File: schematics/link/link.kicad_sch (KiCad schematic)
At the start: 22 parts, among them J1 S2, J2 ARJM11C7-114-BA-EW2, J3 SDI12, J4 S1

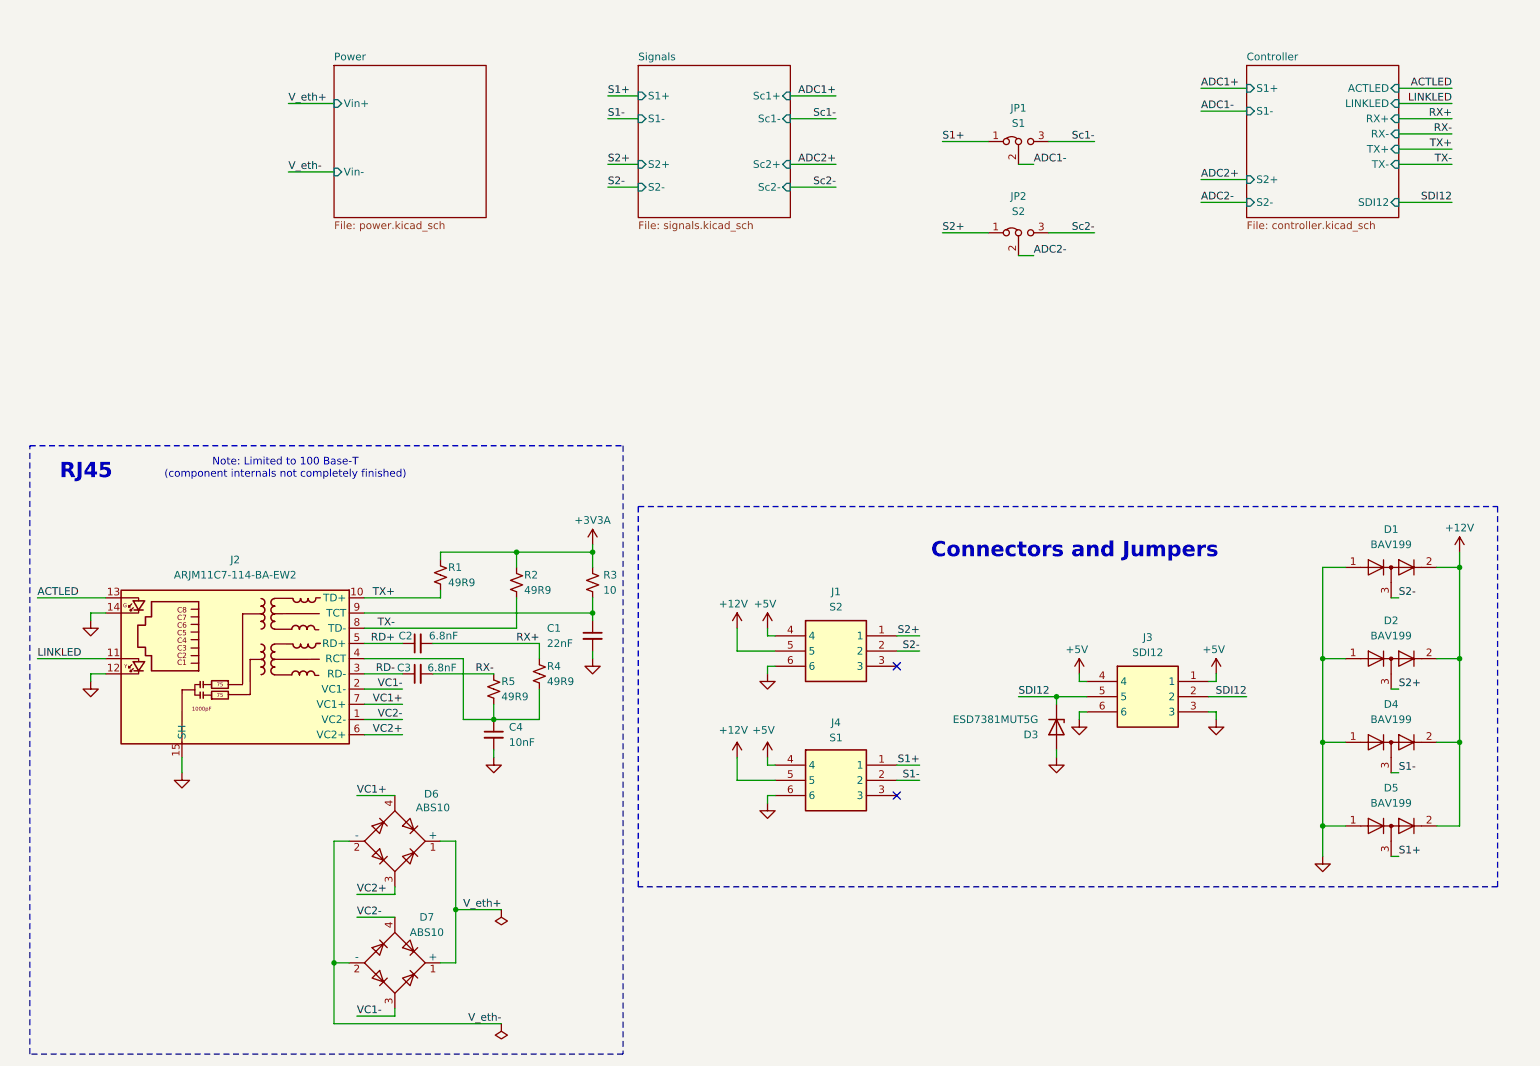
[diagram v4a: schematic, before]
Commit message: update(review):
1. Take gain resistor out of AFE filter
2. Breakout I2C
3. Move fuse to cover both 12V rails
4. Silkscreens
5. More testpoints + change to clip ons
6. Match ADC input max and filter output max
7. Add shunt for current resistors
8. Thermocouples
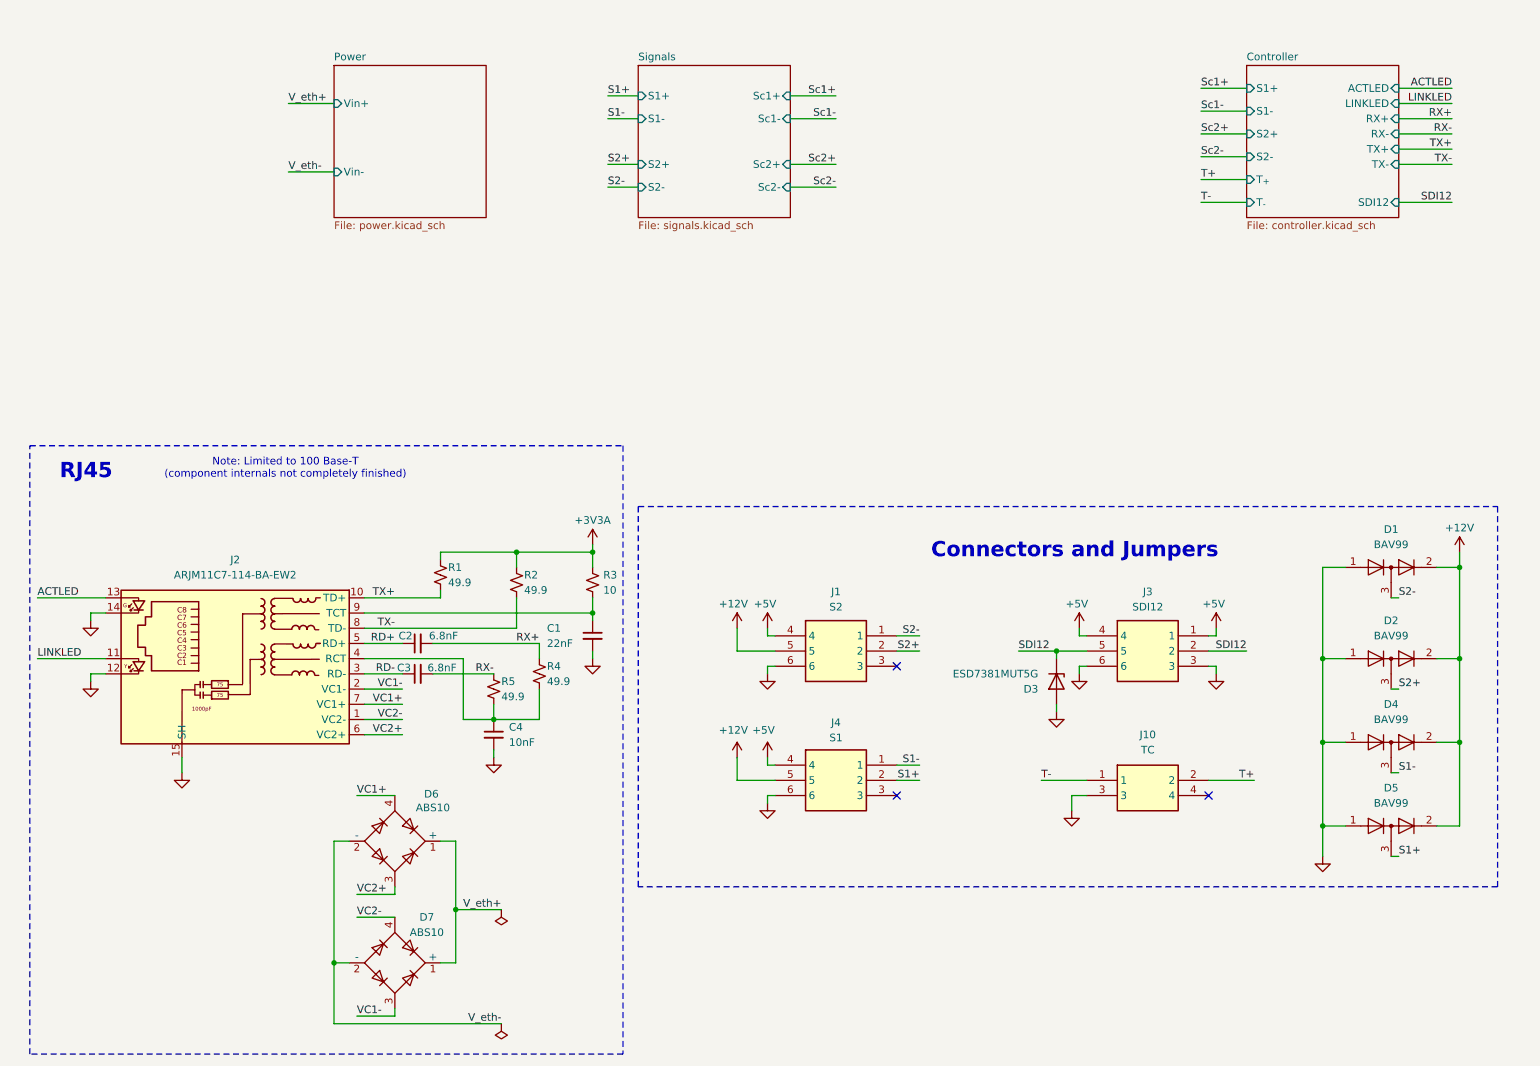
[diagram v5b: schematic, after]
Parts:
- removed JP1: S1, Connector_PinHeader_2.54mm:PinHeader_1x03_P2.54mm_Vertical, symbol Jumper:Jumper_3_Bridged12
- removed JP2: S2, Connector_PinHeader_2.54mm:PinHeader_1x03_P2.54mm_Vertical, symbol Jumper:Jumper_3_Bridged12
- added J10: TC, Link_Footprints:PC-1053864, symbol Link_Components:PC-1053864
- C1: MPN (none) -> GRM155R71H223JA12D
- C2, C3: MPN (none) -> GRM155R71E682KA01D
- C4: MPN (none) -> GRM155R71H103KA88D
- D1, D2, D4, D5: value BAV199 -> BAV99; MPN (none) -> BAV99
- D3: MPN (none) -> ESD7381MUT5G
- D6, D7: MPN (none) -> ABS10
- J1, J3, J4: MPN (none) -> 1053866
- J2: MPN (none) -> ARJM11C7-114-BA-EW2
- R1, R2, R4, R5: value 49R9 -> 49.9; MPN (none) -> RC0402FR-0749R9L
- R3: MPN (none) -> RC0402FR-0710RL
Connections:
- net GND: now also J10.3
- net S1+: now also J4.2; no longer J4.1
- net S1-: now also J4.1; no longer J4.2
- net S2+: now also J1.2; no longer J1.1
- net S2-: now also J1.1; no longer J1.2
- new net T+: J10.2
- new net T-: J10.1
- no-connect marks 2 -> 3
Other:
- sheet Controller ports: added T_{+}, T_{-}; removed none
- moved on the sheet: D3, J3

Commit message: update(connector pinouts)
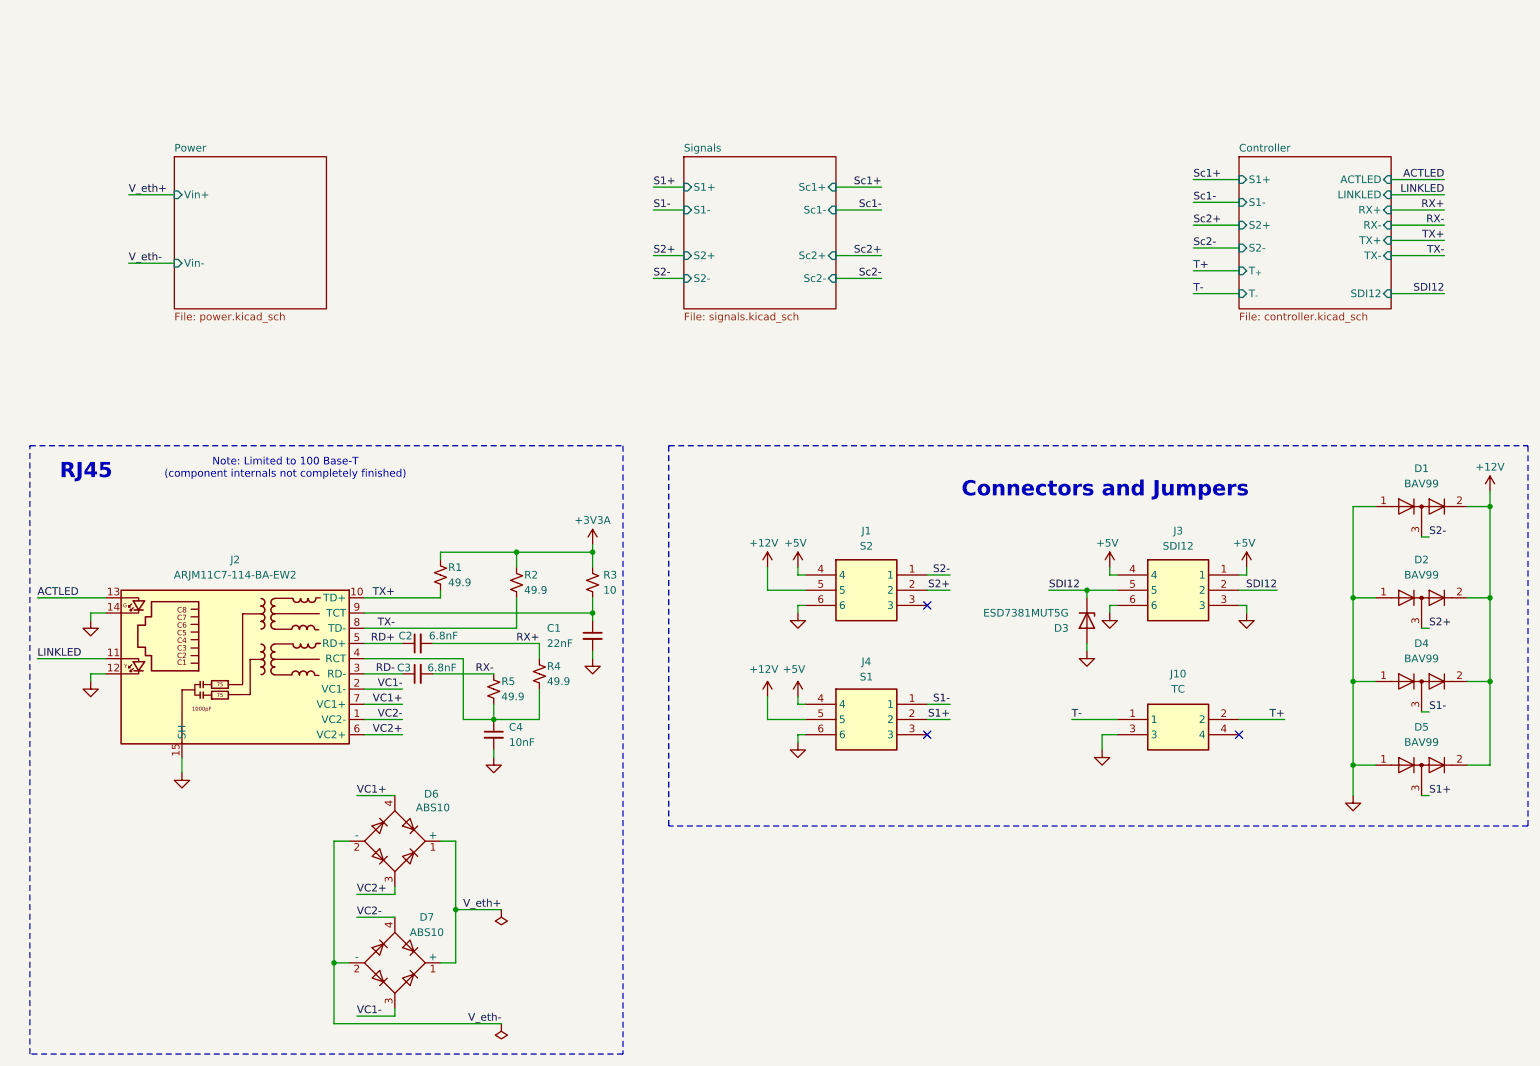
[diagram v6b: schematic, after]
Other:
- company: (none) -> OATS Center
- title: (none) -> Link
- moved on the sheet: D1, D2, D3, D4, D5, J1, J10, J3, J4

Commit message: GPT review
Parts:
- C1: LCSC C21122 -> (none)
- C2, C3, C4: LCSC C57112 -> (none)
- D1, D2, D4, D5: LCSC C155248 -> (none)
- D3: value ESD7381MUT5G -> ESD50VD5; LCSC C2987139 -> (none); MPN ESD7381MUT5G -> ESD5V0D5-TP
- D6, D7: LCSC C19078060 -> (none)
- J1, J3, J4: now in the parts list
- J2: LCSC C6578967 -> (none)
- R1, R2, R3, R4, R5: LCSC C22859 -> (none)
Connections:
- net +3V3A renamed +3V3A1

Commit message: GPT review pt2
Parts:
- R3: MPN RC0402FR-0710RL -> RT0402BRD0710RL
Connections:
- net ACTLED: now also J2.14; no longer J2.13
- net GND: no longer J2.12, J2.14
- net LINKLED: now also J2.12; no longer J2.11
- new net +3V3D: J2.11, J2.13
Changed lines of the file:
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@@
 	)
 	(junction
+		(at 35.56 114.3)
+		(diameter 0)
+		(color 0 0 0 0)
+	)
+	(junction
 		(at 96.52 166.37)
 		(diameter 0)
@@
 	(wire
 		(pts
-			(xy 129.54 49.53) (xy 134.62 49.53)
+			(xy 35.56 111.76) (xy 35.56 114.3)
 		)
 		(stroke
@@
 	(wire
 		(pts
-			(xy 35.56 116.84) (xy 35.56 118.11)
+			(xy 129.54 49.53) (xy 134.62 49.53)
 		)
 		(stroke
@@
 	(wire
 		(pts
-			(xy 38.1 127) (xy 35.56 127)
-		)
-		(stroke
-			(width 0)
-			(type default)
-		)
-	)
-	(wire
-		(pts
 			(xy 153.67 137.16) (xy 154.94 137.16)
 		)
@@
 	(wire
 		(pts
-			(xy 252.73 52.07) (xy 261.62 52.07)
+			(xy 35.56 114.3) (xy 35.56 124.46)
 		)
 		(stroke
@@
 	(wire
 		(pts
-			(xy 81.28 119.38) (xy 106.68 119.38)
+			(xy 252.73 52.07) (xy 261.62 52.07)
 		)
 		(stroke
@@
 	(wire
 		(pts
-			(xy 26.67 114.3) (xy 38.1 114.3)
+			(xy 81.28 119.38) (xy 106.68 119.38)
 		)
 		(stroke
@@
 	(wire
 		(pts
-			(xy 35.56 116.84) (xy 38.1 116.84)
-		)
-		(stroke
-			(width 0)
-			(type default)
-		)
-	)
-	(wire
-		(pts
 			(xy 246.38 114.3) (xy 246.38 128.27)
 		)
@@
 	(wire
 		(pts
+			(xy 26.67 116.84) (xy 38.1 116.84)
+		)
+		(stroke
+			(width 0)
+			(type default)
+		)
+	)
+	(wire
+		(pts
 			(xy 148.59 130.81) (xy 148.59 134.62)
 		)
@@
 	(wire
 		(pts
-			(xy 26.67 124.46) (xy 38.1 124.46)
+			(xy 26.67 127) (xy 38.1 127)
 		)
 		(stroke
@@
 	(wire
 		(pts
-			(xy 35.56 127) (xy 35.56 128.27)
+			(xy 153.67 132.08) (xy 153.67 130.81)
 		)
 		(stroke
@@
 	(wire
 		(pts
-			(xy 153.67 132.08) (xy 153.67 130.81)
+			(xy 246.38 128.27) (xy 246.38 142.24)
 		)
 		(stroke
@@
 	(wire
 		(pts
-			(xy 246.38 128.27) (xy 246.38 142.24)
+			(xy 259.08 147.32) (xy 257.81 147.32)
 		)
 		(stroke
@@
 	(wire
 		(pts
-			(xy 259.08 147.32) (xy 257.81 147.32)
+			(xy 148.59 109.22) (xy 148.59 113.03)
 		)
 		(stroke
@@
 	(wire
 		(pts
-			(xy 148.59 109.22) (xy 148.59 113.03)
+			(xy 81.28 116.84) (xy 119.38 116.84)
 		)
 		(stroke
@@
 	(wire
 		(pts
-			(xy 81.28 116.84) (xy 119.38 116.84)
+			(xy 80.01 147.32) (xy 86.36 147.32)
 		)
 		(stroke
@@
 	(wire
 		(pts
-			(xy 80.01 147.32) (xy 86.36 147.32)
+			(xy 38.1 124.46) (xy 35.56 124.46)
 		)
 		(stroke
@@
 	(wire
 		(pts
+			(xy 38.1 114.3) (xy 35.56 114.3)
+		)
+		(stroke
+			(width 0)
+			(type default)
+		)
+	)
+	(wire
+		(pts
 			(xy 227.33 110.49) (xy 228.6 110.49)
 		)
@@
 	)
 	(label "LINKLED"
-		(at 26.67 124.46 0)
+		(at 26.67 127 0)
 		(effects
 			(font
@@
 	)
 	(label "ACTLED"
-		(at 26.67 114.3 0)
+		(at 26.67 116.84 0)
 		(effects
 			(font
@@
 	)
 	(symbol
-		(lib_id "power:GND")
-		(at 35.56 118.11 0)
-		(mirror y)
-		(unit 1)
-		(body_style 1)
-		(exclude_from_sim no)
-		(in_bom yes)
-		(on_board yes)
-		(in_pos_files yes)
-		(dnp no)
-		(property "Reference" "#PWR03"
-			(at 35.56 124.46 0)
-			(hide yes)
-			(show_name no)
-			(do_not_autoplace no)
-			(effects
-				(font
-					(size 1.27 1.27)
-				)
-			)
-		)
-		(property "Value" "GND"
-			(at 31.496 119.888 0)
-			(hide yes)
-			(show_name no)
-			(do_not_autoplace no)
-			(effects
-				(font
-					(size 1.27 1.27)
-				)
-			)
-		)
-		(property "Footprint" ""
-			(at 35.56 118.11 0)
-			(hide yes)
-			(show_name no)
-			(do_not_autoplace no)
-			(effects
-				(font
-					(size 1.27 1.27)
-				)
-			)
-		)
-		(property "Datasheet" ""
-			(at 35.56 118.11 0)
-			(hide yes)
-			(show_name no)
-			(do_not_autoplace no)
-			(effects
-				(font
-					(size 1.27 1.27)
-				)
-			)
-		)
-		(property "Description" "Power symbol creates a global label with name \"GND\" , ground"
-			(at 35.56 118.11 0)
-			(hide yes)
-			(show_name no)
-			(do_not_autoplace no)
-			(effects
-				(font
-					(size 1.27 1.27)
-				)
-			)
-		)
-		(pin "1"
-		)
-		(instances
-			(project "link"
-				(path "/e6a73b1b-9233-47b9-8d6b-253608bed688"
-					(reference "#PWR03")
-					(unit 1)
-				)
-			)
-		)
-	)
-	(symbol
 		(lib_id "power:+12V")
 		(at 148.59 130.81 0)
@@
 			)
 		)
-		(property "MPN" "RC0402FR-0710RL"
+		(property "MPN" "RT0402BRD0710RL"
 			(at 119.38 111.76 0)
 			(hide yes)
@@
 	(symbol
 		(lib_id "power:GND")
-		(at 35.56 128.27 0)
-		(mirror y)
-		(unit 1)
-		(body_style 1)
-		(exclude_from_sim no)
-		(in_bom yes)
-		(on_board yes)
-		(in_pos_files yes)
-		(dnp no)
-		(property "Reference" "#PWR010"
-			(at 35.56 134.62 0)
-			(hide yes)
-			(show_name no)
-			(do_not_autoplace no)
-			(effects
-				(font
-					(size 1.27 1.27)
-				)
-			)
-		)
-		(property "Value" "GND"
-			(at 31.496 130.048 0)
-			(hide yes)
-			(show_name no)
-			(do_not_autoplace no)
-			(effects
-				(font
-					(size 1.27 1.27)
-				)
-			)
-		)
-		(property "Footprint" ""
-			(at 35.56 128.27 0)
-			(hide yes)
-			(show_name no)
-			(do_not_autoplace no)
-			(effects
-				(font
-					(size 1.27 1.27)
-				)
-			)
-		)
-		(property "Datasheet" ""
-			(at 35.56 128.27 0)
-			(hide yes)
-			(show_name no)
-			(do_not_autoplace no)
-			(effects
-				(font
-					(size 1.27 1.27)
-				)
-			)
-		)
-		(property "Description" "Power symbol creates a global label with name \"GND\" , ground"
-			(at 35.56 128.27 0)
-			(hide yes)
-			(show_name no)
-			(do_not_autoplace no)
-			(effects
-				(font
-					(size 1.27 1.27)
-				)
-			)
-		)
-		(pin "1"
-		)
-		(instances
-			(project "link"
-				(path "/e6a73b1b-9233-47b9-8d6b-253608bed688"
-					(reference "#PWR010")
-					(unit 1)
-				)
-			)
-		)
-	)
-	(symbol
-		(lib_id "power:GND")
 		(at 153.67 116.84 0)
 		(mirror y)
@@
 					(unit 1)
 				)
+			)
+		)
+	)
+	(symbol
+		(lib_id "power:+3V3")
+		(at 35.56 111.76 0)
+		(unit 1)
+		(body_style 1)
+		(exclude_from_sim no)
+		(in_bom yes)
+		(on_board yes)
+		(in_pos_files yes)
+		(dnp no)
+		(property "Reference" "#PWR0105"
+			(at 35.56 115.57 0)
+			(hide yes)
+			(show_name no)
+			(do_not_autoplace no)
+			(effects
+				(font
+					(size 1.27 1.27)
+				)
+			)
+		)
+		(property "Value" "+3V3D"
+			(at 35.306 107.696 0)
+			(show_name no)
+			(do_not_autoplace no)
+			(effects
+				(font
+					(size 1.27 1.27)
+				)
+			)
+		)
+		(property "Footprint" ""
+			(at 35.56 111.76 0)
+			(hide yes)
+			(show_name no)
+			(do_not_autoplace no)
+			(effects
+				(font
+					(size 1.27 1.27)
+				)
+			)
+		)
+		(property "Datasheet" ""
+			(at 35.56 111.76 0)
+			(hide yes)
+			(show_name no)
+			(do_not_autoplace no)
+			(effects
+				(font
+					(size 1.27 1.27)
+				)
+			)
+		)
+		(property "Description" "Power symbol creates a global label with name \"+3V3\""
+			(at 35.56 111.76 0)
+			(hide yes)
+			(show_name no)
+			(do_not_autoplace no)
+			(effects
+				(font
+					(size 1.27 1.27)
+				)
+			)
+		)
+		(pin "1"
+		)
+		(instances
+			(project "link"
+				(path "/e6a73b1b-9233-47b9-8d6b-253608bed688"
+					(reference "#PWR0105")
+					(unit 1)
+				)
